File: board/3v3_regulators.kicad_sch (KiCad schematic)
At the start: 5 parts, among them U501 AP7342

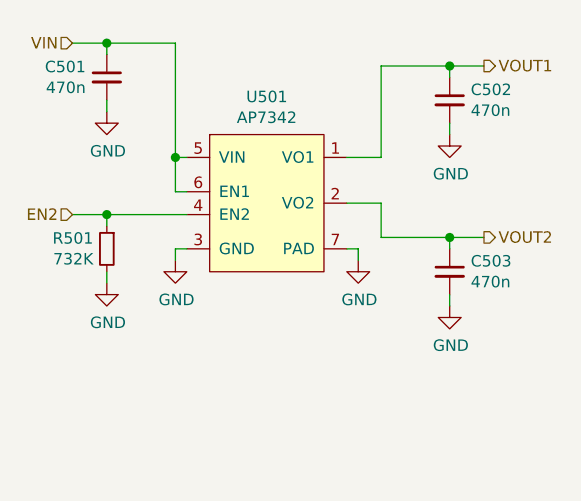
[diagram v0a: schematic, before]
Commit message: Added testpoints and other fixes
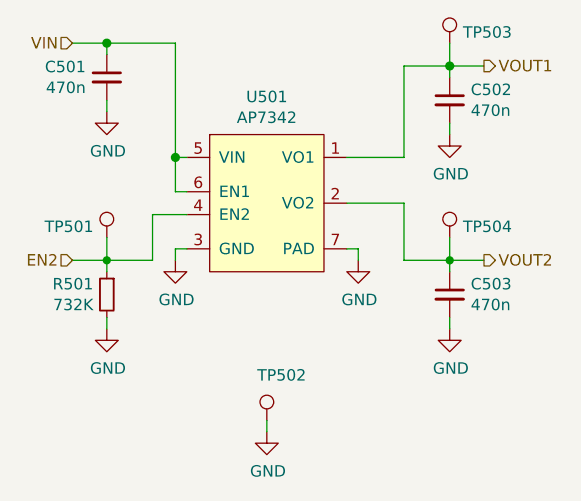
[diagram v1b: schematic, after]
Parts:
- added TP501, TP502, TP503, TP504: TestPoint, DIYPie:TestPoint_Pad_D1.5mm, symbol DIYPie:TestPoint
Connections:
- net EN2: now also TP501.1
- net GND: now also TP502.1
- net VOUT1: now also TP503.1
- net VOUT2: now also TP504.1
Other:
- moved on the sheet: C503, R501
